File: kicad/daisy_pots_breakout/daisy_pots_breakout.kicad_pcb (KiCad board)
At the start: 2 copper layers, 100 x 26 mm, 6 parts, among them J1 Conn_01x11_Pin, SW1 RotaryEncoder_Switch

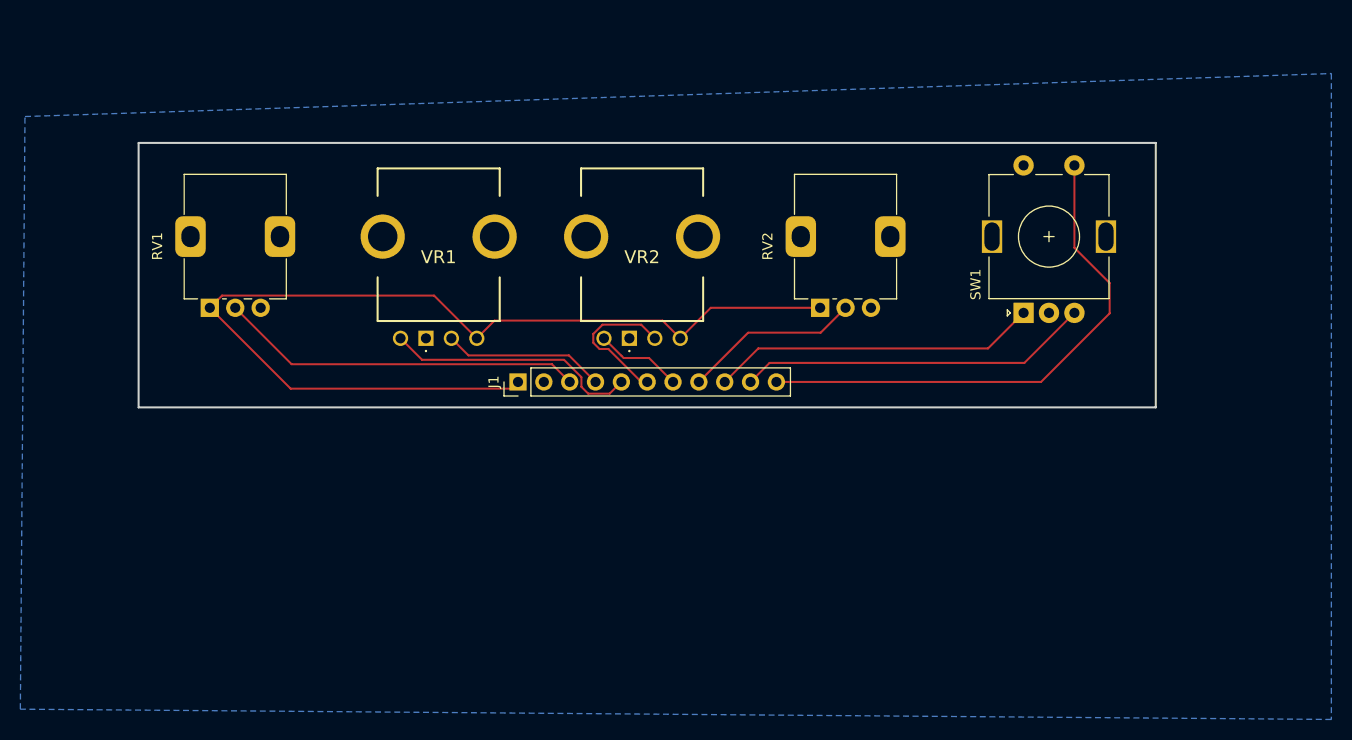
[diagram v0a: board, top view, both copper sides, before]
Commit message: Make side boards for pots and buttons use same connector as main board
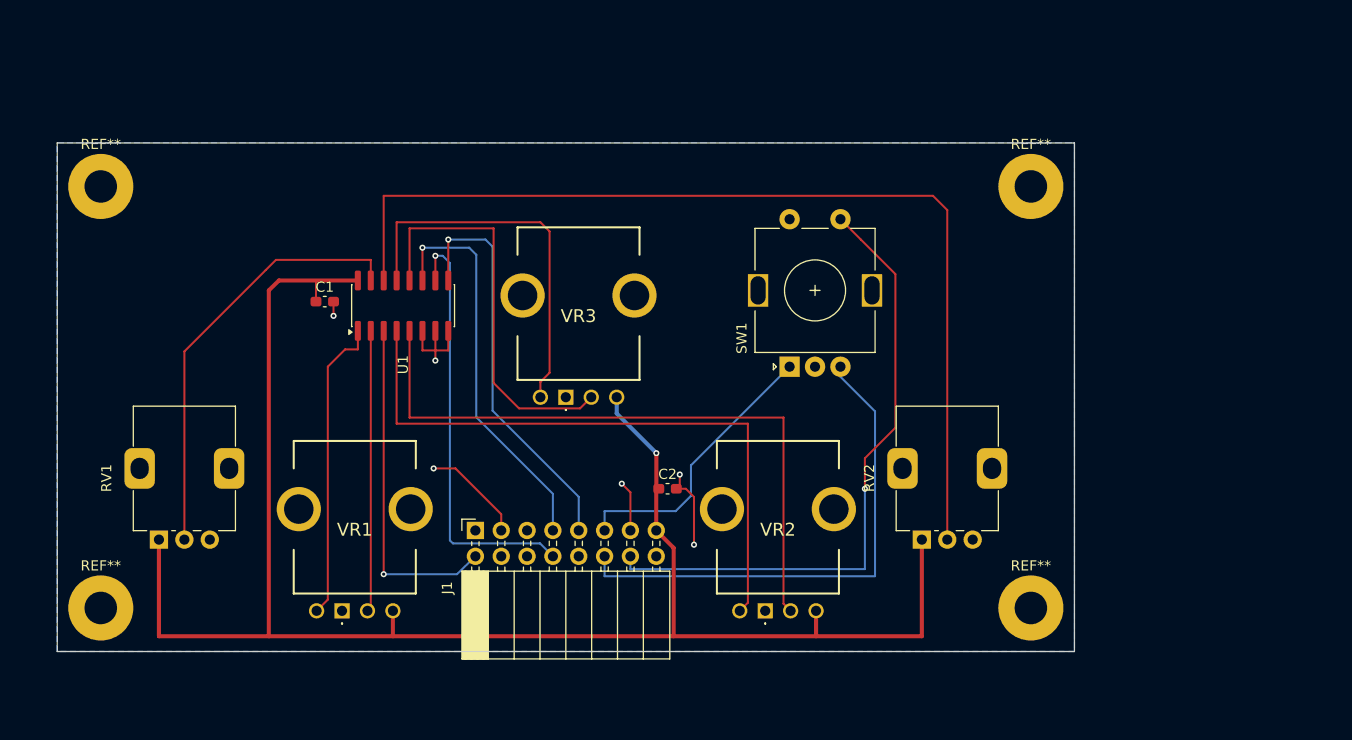
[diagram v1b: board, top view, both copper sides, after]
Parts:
- added C1: 100nF, C_0603_1608Metric_Pad1.08x0.95mm_HandSolder, F.Cu at (76.3, 65.6)
- added C2: 10uF, C_0603_1608Metric_Pad1.08x0.95mm_HandSolder, F.Cu at (110.0, 84.0)
- added REF**: MountingHole_3.2mm_M3_Pad, MountingHole_3.2mm_M3_Pad, F.Cu at (54.3, 54.3)
- added REF**: MountingHole_3.2mm_M3_Pad, MountingHole_3.2mm_M3_Pad, F.Cu at (54.3, 95.7)
- added REF**: MountingHole_3.2mm_M3_Pad, MountingHole_3.2mm_M3_Pad, F.Cu at (145.7, 54.3)
- added REF**: MountingHole_3.2mm_M3_Pad, MountingHole_3.2mm_M3_Pad, F.Cu at (145.7, 95.7)
- added U1: 74HC4051D, SOIC-16_3.9x9.9mm_P1.27mm, F.Cu at (84.0, 66.0)
- added VR3: RV112FF-40B1, RV112FF:RV112FF40B115F0B20K0068, F.Cu at (100.0, 75.0)
- J1: value Conn_01x11_Pin -> Petal_2x08; footprint Connector_PinHeader_2.54mm:PinHeader_1x11_P2.54mm_Vertical -> PinSocket_2x08_P2.54mm_Horizontal
- RV1, RV2: value R_Potentiometer -> 10k
- SW1: value RotaryEncoder_Switch -> EC11E
- VR1, VR2: value RV112FF-40B1-15F-0B20K-0068 -> RV112FF-40B1
- moved VR2 29.9 mm to (119.6, 96.0)
- moved VR1 28.0 mm to (78.0, 96.0)
- moved RV2 24.9 mm to (135.0, 89.0)
- moved SW1 23.6 mm to (122.0, 72.0)
- moved RV1 23.3 mm to (60.0, 89.0)
- moved J1 15.2 mm to (91.1, 88.1)
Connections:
- J1 pad 1: +3V3 -> GND
- J1 pad 10: /ROT_B -> unconnected-(J1-Pin_10-Pad10)
- J1 pad 11: /ROT_S -> /ENC_A
- J1 pad 2: GND -> /ADC
- J1 pad 3: /LP_1 -> GND
- J1 pad 4: /RV1_1 -> unconnected-(J1-Pin_4-Pad4)
- J1 pad 5: /RV1_2 -> unconnected-(J1-Pin_5-Pad5)
- J1 pad 6: /RV2_1 -> unconnected-(J1-Pin_6-Pad6)
- J1 pad 7: /RV2_2 -> /A_S0
- J1 pad 8: /LP_2 -> /A_S1
- J1 pad 9: /ROT_A -> /A_S2
- RV1 pad 1: +3V3 -> +3.3VA
- RV1 pad 2: /LP_1 -> /POT1
- RV2 pad 1: +3V3 -> +3.3VA
- RV2 pad 2: /LP_2 -> /POT2
- SW1 pad A: /ROT_A -> /ENC_A
- SW1 pad B: /ROT_B -> /ENC_B
- SW1 pad S1: /ROT_S -> /ENC_SW
- VR1 pad 2: /RV1_1 -> /JOY1_X
- VR1 pad 3: +3V3 -> +3.3VA
- VR1 pad A2: /RV1_2 -> /JOY1_Y
- VR2 pad 2: /RV2_1 -> /JOY2_X
- VR2 pad 3: +3V3 -> +3.3VA
- VR2 pad A2: /RV2_2 -> /JOY2_Y
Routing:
- net +3.3VA: track 0.00 -> 170.2 mm, vias 0 -> 1
- net +3V3: track 98.8 -> 0.00 mm
- net /POT2: track 0.00 -> 96.7 mm
- net /JOY2_X: track 0.00 -> 64.6 mm
- net /JOY2_Y: track 0.00 -> 62.4 mm
- net /ENC_SW: track 0.00 -> 62.2 mm, vias 0 -> 1
- net /ROT_S: track 51.5 -> 0.00 mm
- net /ENC_B: track 0.00 -> 50.6 mm
- net /POT1: track 0.00 -> 42.6 mm
- net /A_S1: track 0.00 -> 42.2 mm, vias 0 -> 1
- net /A_S2: track 0.00 -> 40.1 mm, vias 0 -> 1
- net /JOY3_X: track 0.00 -> 39.7 mm
- net /A_S0: track 0.00 -> 39.0 mm, vias 0 -> 1
- net /JOY3_Y: track 0.00 -> 37.8 mm
- net /LP_1: track 35.9 -> 0.00 mm
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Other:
- board size 100 x 26 mm -> 100 x 50 mm

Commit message: Finish breakout periph boards and add gerbers
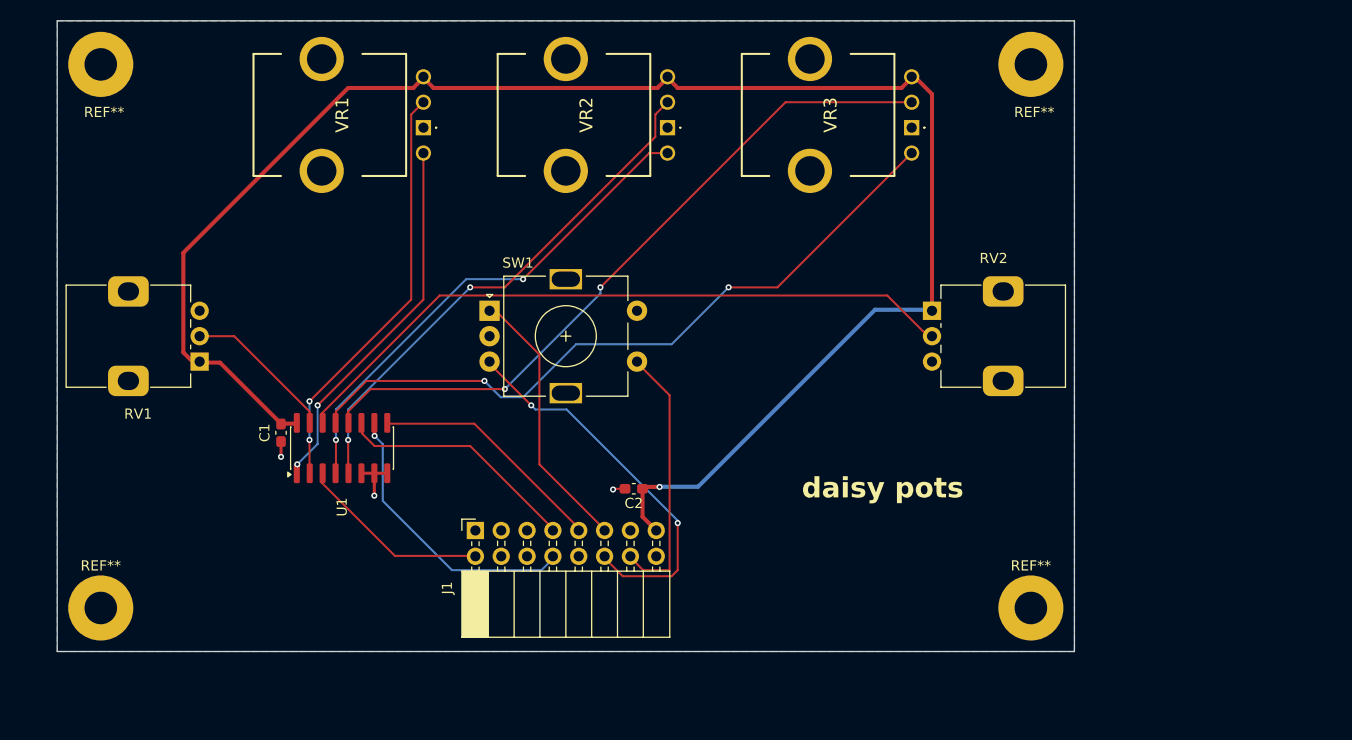
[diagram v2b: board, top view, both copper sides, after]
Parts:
- moved VR2 48.5 mm to (110.0, 48.5), turned to 90 degrees
- moved VR1 48.2 mm to (86.0, 48.5), turned to 90 degrees
- moved VR3 43.1 mm to (134.0, 48.5), turned to 90 degrees
- moved SW1 30.0 mm to (92.5, 66.5), turned to 0 degrees
- moved RV2 22.5 mm to (136.0, 66.5), turned to 0 degrees
- moved RV1 18.0 mm to (64.0, 71.5), turned to 180 degrees
- moved U1 15.2 mm to (78.0, 80.0)
- moved C1 13.6 mm to (72.0, 78.5), turned to -90 degrees
- moved REF** 12.0 mm to (54.3, 42.3)
- moved REF** 12.0 mm to (145.7, 42.3)
- moved C2 3.32 mm to (106.7, 84.0), turned to 180 degrees
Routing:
- net /ENC_SW: track 62.2 -> 26.4 mm, vias 1 -> 0
- net /JOY3_Y: track 37.8 -> 69.7 mm, vias 0 -> 2
- net /JOY3_X: track 39.7 -> 69.6 mm, vias 0 -> 2
- net /POT2: track 96.7 -> 67.6 mm
- net /POT1: track 42.6 -> 15.1 mm
- net GND: track 34.1 -> 7.44 mm, vias 6 -> 3
- net /A_S2: track 40.1 -> 23.4 mm, vias 1 -> 0
- net /A_S0: track 39.0 -> 23.9 mm, vias 1 -> 0
- net /ADC: track 33.7 -> 19.4 mm, vias 1 -> 0
- net /A_S1: track 42.2 -> 28.4 mm
- net /JOY1_X: track 27.7 -> 41.1 mm, vias 0 -> 2
- net /JOY2_X: track 64.6 -> 51.5 mm, vias 0 -> 2
- net /JOY2_Y: track 62.4 -> 49.3 mm, vias 0 -> 2
- net /ENC_B: track 50.6 -> 38.5 mm, vias 0 -> 2
- net /JOY1_Y: track 29.9 -> 36.6 mm, vias 0 -> 2
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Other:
- board size 100 x 50 mm -> 100 x 62 mm
- board text added: "daisy pots"
